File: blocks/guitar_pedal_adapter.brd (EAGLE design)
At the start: 37 x 33 mm, 36 parts, among them IC1 TL072P, IC2 LM7809

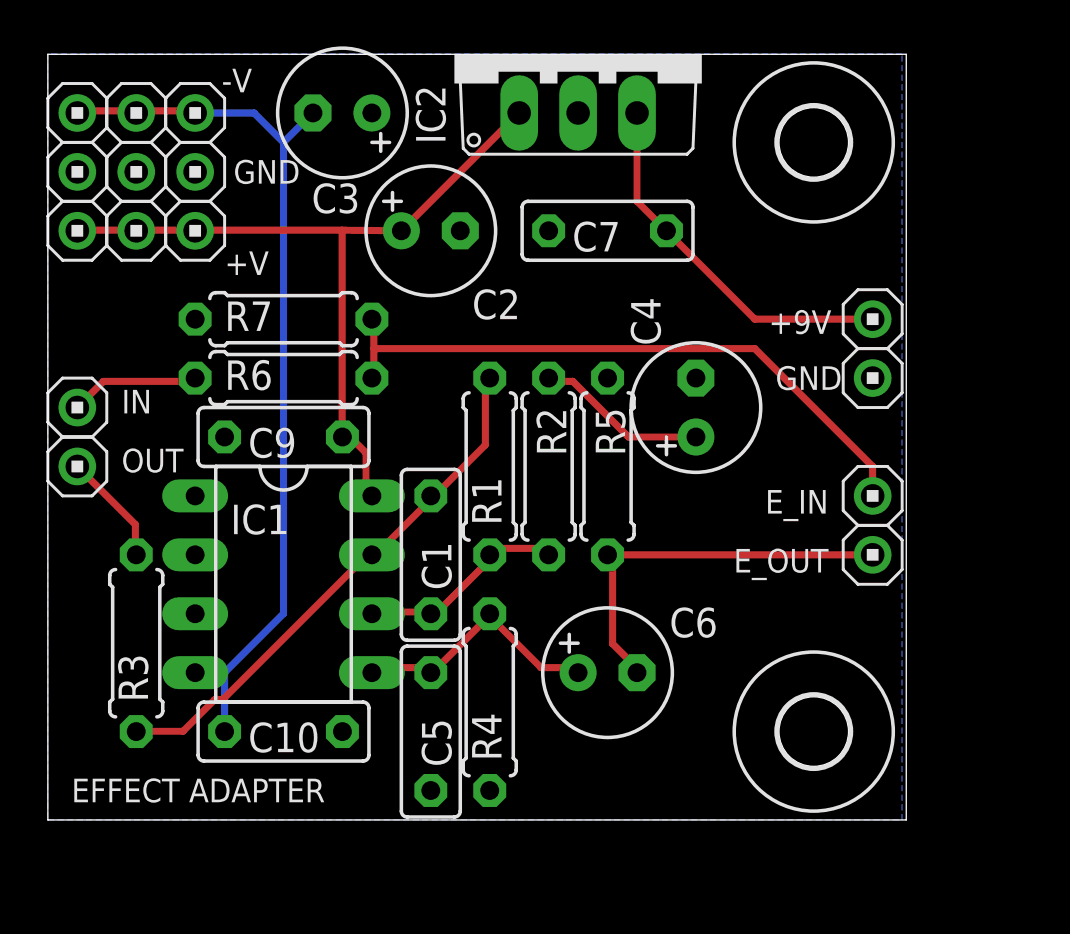
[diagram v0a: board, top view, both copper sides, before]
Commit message: Added low pass/band pass filter block
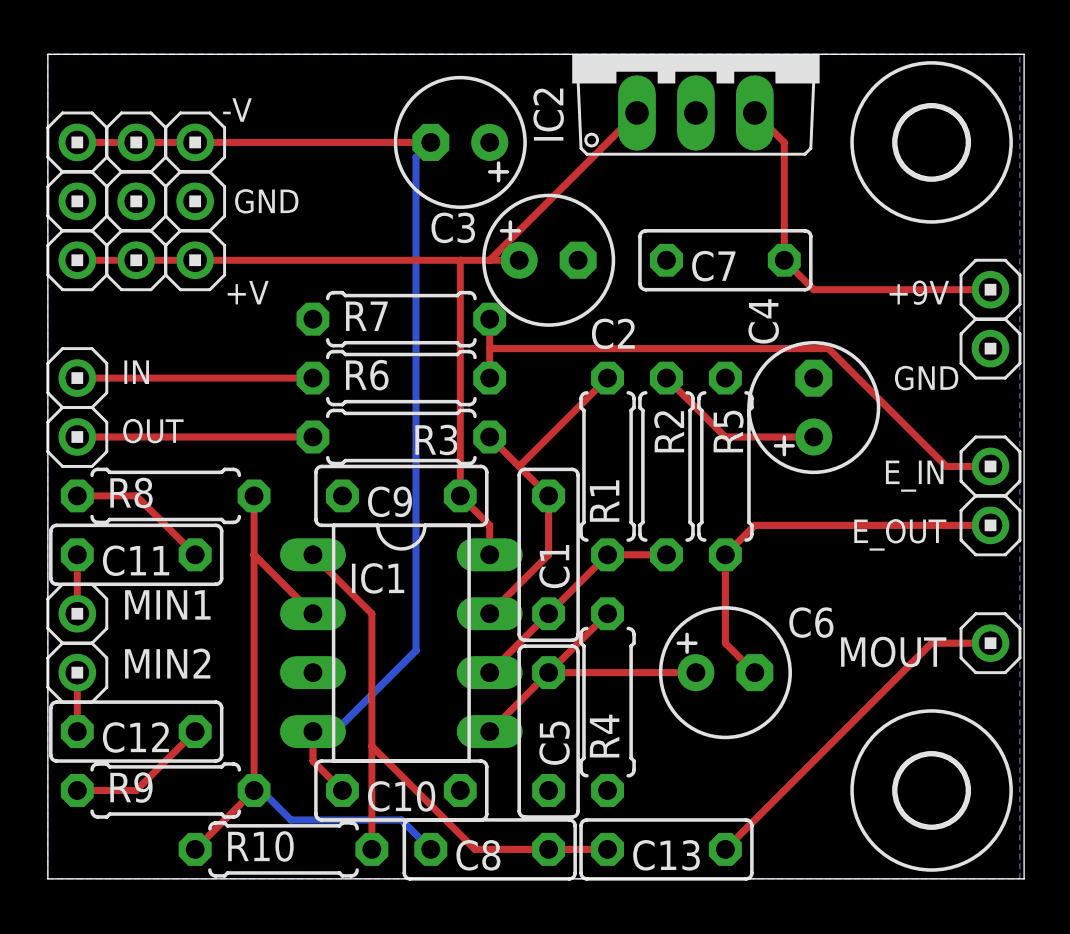
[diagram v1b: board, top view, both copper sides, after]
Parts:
- added C11, C12: 0.1uF, capacitors:CERAMICDISC/5
- added C13: 2uF, capacitors:CERAMICDISC/5
- added C8: 47pF, capacitors:CERAMICDISC/5
- added MIN1, MIN2, MOUT: HEADER/MALE/01, connectors:HEADER/MALE/01
- added R10, R8, R9: 100k, resistors:RESISTOR/7.5
- moved R3 14.5 mm to (15.2, 34.3), turned to 180 degrees
- moved IC1 5.68 mm to (15.2, 25.4)
- moved C10 5.68 mm to (15.2, 19.1)
- moved C9 5.68 mm to (15.2, 31.8)
- moved U$1 5.68 mm to (38.1, 19.1)
- moved C7 5.24 mm to (29.2, 41.9)
- moved C3 5.24 mm to (17.8, 47.0)
- moved +9V 5.24 mm to (40.6, 40.6)
- moved C2 5.24 mm to (21.6, 41.9)
- moved E_IN 5.24 mm to (40.6, 33.0)
- moved GND4 5.24 mm to (40.6, 38.1)
- moved U$3 5.24 mm to (37.6, 33.8)
- moved E_OUT 5.24 mm to (40.6, 30.5)
- moved C4 5.08 mm to (33.0, 35.6)
- moved C6 5.08 mm to (29.2, 24.1)
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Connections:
- new net N$10: C8.1, IC1.2, R10.1, R8.2, R9.2
- new net N$11: C13.1, C8.2, IC1.1, R10.2
- new net N$12: C13.2, MOUT.1
- new net N$13: C11.2, R8.1
- new net N$14: C12.2, R9.1
- new net N$15: C11.1, MIN1.1
- new net N$16: C12.1, MIN2.1
- net GND: now also IC1.3
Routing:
- net N$10: track 0.00 -> 28.6 mm
- net N$11: track 0.00 -> 25.8 mm
- net N$12: track 0.00 -> 15.1 mm
- net N$1: track 23.2 -> 15.1 mm
- net +12V: track 33.4 -> 41.3 mm
- net -12V: track 39.1 -> 46.4 mm
- net N$14: track 0.00 -> 6.13 mm
- net N$13: track 0.00 -> 6.13 mm
- net N$9: track 4.85 -> 10.2 mm
- net N$6: track 5.60 -> 10.2 mm
- net N$16: track 0.00 -> 2.54 mm
- net N$15: track 0.00 -> 2.54 mm
- net N$4: track 11.4 -> 13.5 mm
- net N$5: track 27.4 -> 26.2 mm
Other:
- board size 37 x 33 mm -> 42.1 x 35.5 mm
